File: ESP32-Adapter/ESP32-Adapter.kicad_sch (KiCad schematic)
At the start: 17 parts, among them J10 Barrel_Jack, J12 Conn_01x05, J13 Conn_01x05, J2 Conn_01x03, J3 Conn_01x03, J5 Conn_01x03, U1 ESP32-C5-DevKitC-1, U2 LM317DCYR, U3 Adafruit CANPAL, U4 ADAFRUIT INA219 BREAKOUT

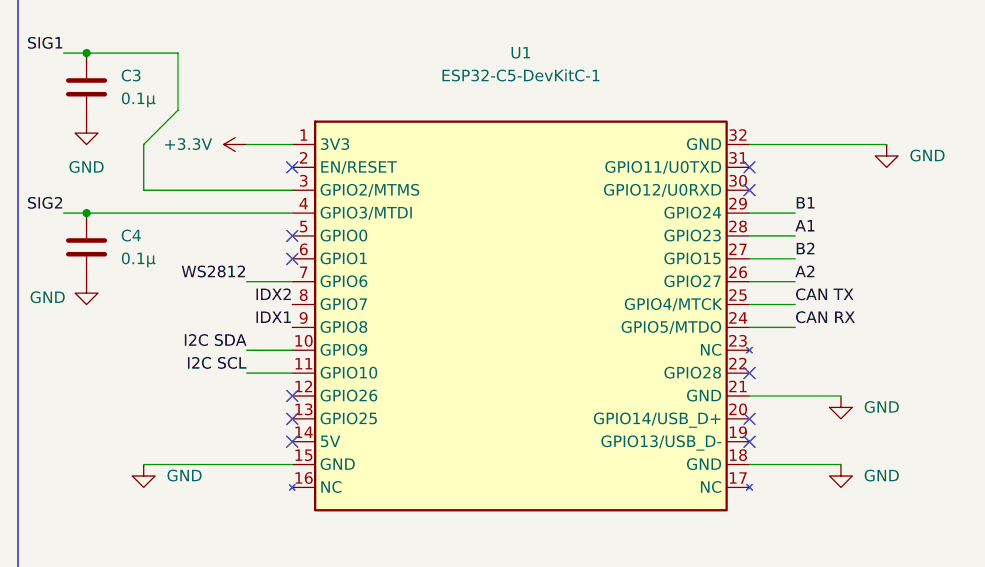
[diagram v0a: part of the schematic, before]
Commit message: fix schematic, symbols, footprints
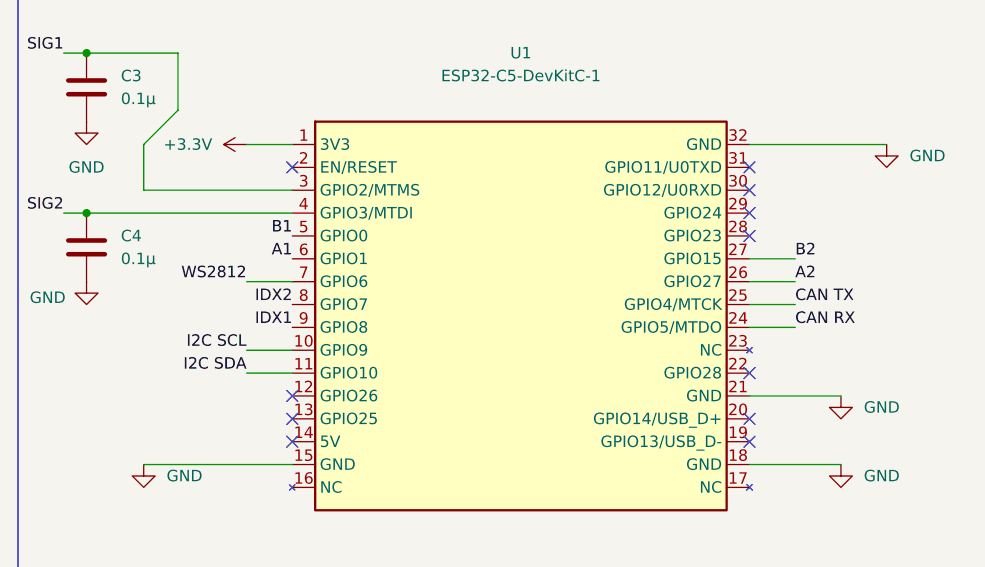
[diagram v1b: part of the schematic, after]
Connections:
- net A1: now also U1.6 (GPIO1); no longer U1.28 (GPIO23)
- net B1: now also U1.5 (GPIO0); no longer U1.29 (GPIO24)
- net I2C SCL: now also U1.10 (GPIO9); no longer U1.11 (GPIO10)
- net I2C SDA: now also U1.11 (GPIO10); no longer U1.10 (GPIO9)
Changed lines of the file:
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@@
+	)
+	(no_connect
+		(at 215.9 148.59)
 	)
 	(no_connect
@@
 	)
 	(no_connect
+		(at 215.9 146.05)
+	)
+	(no_connect
 		(at 165.1 171.45)
 	)
@@
 	)
 	(no_connect
-		(at 165.1 148.59)
-	)
-	(no_connect
 		(at 165.1 168.91)
 	)
@@
 	)
 	(no_connect
-		(at 165.1 151.13)
-	)
-	(no_connect
 		(at 110.49 179.07)
 	)
@@
 	(wire
 		(pts
-			(xy 215.9 146.05) (xy 220.98 146.05)
-		)
-		(stroke
-			(width 0)
-			(type default)
-		)
-	)
-	(wire
-		(pts
 			(xy 215.9 138.43) (xy 231.14 138.43)
 		)
@@
 		(pts
 			(xy 160.02 153.67) (xy 165.1 153.67)
-		)
-		(stroke
-			(width 0)
-			(type default)
-		)
-	)
-	(wire
-		(pts
-			(xy 215.9 148.59) (xy 220.98 148.59)
 		)
 		(stroke
@@
 		)
 	)
-	(label "I2C SCL"
-		(at 160.02 163.83 180)
-		(effects
-			(font
-				(size 1.27 1.27)
-			)
-			(justify right bottom)
-		)
-	)
-	(label "B1"
-		(at 220.98 146.05 0)
-		(effects
-			(font
-				(size 1.27 1.27)
-			)
-			(justify left bottom)
-		)
-	)
 	(label "B2"
 		(at 111.76 158.75 0)
@@
 	)
 	(label "B1"
+		(at 165.1 148.59 180)
+		(effects
+			(font
+				(size 1.27 1.27)
+			)
+			(justify right bottom)
+		)
+	)
+	(label "B1"
 		(at 111.76 143.51 0)
 		(effects
@@
 		)
 	)
+	(label "I2C SDA"
+		(at 160.02 163.83 180)
+		(effects
+			(font
+				(size 1.27 1.27)
+			)
+			(justify right bottom)
+		)
+	)
 	(label "B2"
 		(at 220.98 151.13 0)
@@
 		)
 	)
-	(label "A1"
-		(at 220.98 148.59 0)
-		(effects
-			(font
-				(size 1.27 1.27)
-			)
-			(justify left bottom)
-		)
-	)
 	(label "CAN TX"
 		(at 220.98 156.21 0)
@@
 		)
 	)
+	(label "A1"
+		(at 165.1 151.13 180)
+		(effects
+			(font
+				(size 1.27 1.27)
+			)
+			(justify right bottom)
+		)
+	)
 	(label "I2C SCL"
 		(at 273.05 193.04 180)
@@
 		)
 	)
+	(label "I2C SCL"
+		(at 160.02 161.29 180)
+		(effects
+			(font
+				(size 1.27 1.27)
+			)
+			(justify right bottom)
+		)
+	)
 	(label "IDX1"
 		(at 111.76 138.43 0)
@@
 		)
 	)
-	(label "I2C SDA"
-		(at 160.02 161.29 180)
-		(effects
-			(font
-				(size 1.27 1.27)
-			)
-			(justify right bottom)
-		)
-	)

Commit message: updates updates
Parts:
- removed C3, C4: 0.1µ, Capacitor_SMD:C_0402_1005Metric, symbol Device:C
- removed J2, J3: Conn_01x03, Connector_JST:JST_XH_S3B-XH-A-1_1x03_P2.50mm_Horizontal, symbol Connector_Generic:Conn_01x03
- removed U1: ESP32-C5-DevKitC-1, PCM_Espressif:ESP32-C5-DevKitC-1, symbol PCM_Espressif:ESP32-C5-DevKitC-1
- added J1, J2, J3: last resort, symbol Connector:Conn_01x01_Socket
- added U1: ICM-42670-P_Click, symbol Sensor_Motion:ICM-42670-P_Click
- added U5: ESP32-S3-DevKitC, PCM_Espressif:ESP32-S3-DevKitC, symbol PCM_Espressif:ESP32-S3-DevKitC
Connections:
- net +3.3V: now also U5.1 (3V3), U5.2 (3V3)
- net A1: now also U5.18 (GPIO12/ADC2_CH1)
- net A2: now also J13.2 (Pin_2), U5.19 (GPIO13/ADC2_CH2); no longer J12.3 (Pin_3)
- net B1: now also J12.3 (Pin_3), U5.8 (GPIO15/ADC2_CH4/32K_P); no longer J13.2 (Pin_2)
- net B2: now also U5.9 (GPIO16/ADC2_CH5/32K_N)
- net CAN RX: now also U5.6 (GPIO6/ADC1_CH5)
- net CAN TX: now also U5.5 (GPIO5/ADC1_CH4)
- net GND: now also U1.16 (GND), U1.8 (GND), U5.22 (GND), U5.23 (GND), U5.24 (GND), U5.44 (GND)
- net I2C SCL: now also U5.15 (GPIO9/ADC1_CH8)
- net I2C SDA: now also U5.16 (GPIO10/ADC1_CH9)
- net WS2812: now also U5.10 (GPIO17/ADC2_CH6)
- net IDX1 renamed IDXA
- net IDXA: now also U5.17 (GPIO11/ADC2_CH0)
- net IDX2 renamed IDXB
- net IDXB: now also U5.7 (GPIO7/ADC1_CH6)
- new net: J1.1 (Pin_1), U5.32 (GPIO35)
- new net: J2.1 (Pin_1), U5.33 (GPIO36)
- new net: J3.1 (Pin_1), U5.34 (GPIO37)
- no-connect marks 16 -> 20
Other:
- note added: "ICM-42670 IMU"
- note removed: "Analog"
- note removed: "Analog 1"
- note removed: "Analog 2"
- note removed: "Vcc"
- moved on the sheet: C1, C2, D1, J10, J12, J13, J5, R1, R2, U2, U3, U4

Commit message: austne yun pins adjusted
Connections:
- net CAN RX: now also U5.41 (GPIO1/ADC1_CH0); no longer U5.6 (GPIO6/ADC1_CH5)
- net CAN TX: now also U5.40 (GPIO2/ADC1_CH1); no longer U5.5 (GPIO5/ADC1_CH4)
- net I2C SCL: no longer U5.15 (GPIO9/ADC1_CH8)
- net I2C SDA: no longer U5.16 (GPIO10/ADC1_CH9)
- net IMU SCL: now reaches U1.13 (SCL)
- net IMU SCL: now also U5.15 (GPIO9/ADC1_CH8)
- net IMU SDA: now reaches U1.14 (SDA)
- net IMU SDA: now also U5.16 (GPIO10/ADC1_CH9)
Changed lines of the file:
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@@
+		)
+	)
+	(label "IMU SCL"
+		(at 115.57 213.36 0)
+		(effects
+			(font
+				(size 1.27 1.27)
+			)
+			(justify left bottom)
 		)
 	)
 	(label "A2"
 		(at 111.76 125.73 0)
+		(effects
+			(font
+				(size 1.27 1.27)
+			)
+			(justify left bottom)
+		)
+	)
+	(label "IMU SDA"
+		(at 115.57 215.9 0)
+		(effects
+			(font
+				(size 1.27 1.27)
+			)
+			(justify left bottom)
+		)
+	)
+	(label "IMU SCL"
+		(at 212.09 175.26 0)
+		(effects
+			(font
+				(size 1.27 1.27)
+			)
+			(justify left bottom)
+		)
+	)
+	(label "CAN RX"
+		(at 212.09 154.94 0)
+		(effects
+			(font
+				(size 1.27 1.27)
+			)
+			(justify left bottom)
+		)
+	)
+	(label "IMU SDA"
+		(at 212.09 177.8 0)
 		(effects
 			(font
@@
 			)
 			(justify right bottom)
-		)
-	)
-	(label "I2C SCL"
-		(at 212.09 175.26 0)
-		(effects
-			(font
-				(size 1.27 1.27)
-			)
-			(justify left bottom)
 		)
 	)
@@
 		)
 	)
-	(label "CAN TX"
-		(at 212.09 165.1 0)
-		(effects
-			(font
-				(size 1.27 1.27)
-			)
-			(justify left bottom)
-		)
-	)
 	(label "B2"
 		(at 161.29 144.78 180)
@@
 			)
 			(justify right bottom)
+		)
+	)
+	(label "I2C SDA"
+		(at 222.25 217.17 0)
+		(effects
+			(font
+				(size 1.27 1.27)
+			)
+			(justify left bottom)
 		)
 	)
@@
 		)
 	)
-	(label "CAN RX"
-		(at 212.09 167.64 0)
+	(label "I2C SCL"
+		(at 222.25 214.63 0)
 		(effects
 			(font
@@
 		)
 	)
-	(label "I2C SDA"
-		(at 212.09 177.8 0)
+	(label "CAN TX"
+		(at 110.49 168.91 0)
 		(effects
 			(font
@@
 	)
 	(label "CAN TX"
-		(at 110.49 168.91 0)
+		(at 212.09 157.48 0)
 		(effects
 			(font

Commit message: connect v sensor pins:
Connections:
- net IMU SCL is gone; now on net I2C SCL: U1.13 (SCL), U5.15 (GPIO9/ADC1_CH8)
- net IMU SDA is gone; now on net I2C SDA: U1.14 (SDA), U5.16 (GPIO10/ADC1_CH9)
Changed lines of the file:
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@@
+	)
+	(junction
+		(at 218.44 177.8)
+		(diameter 0)
+		(color 0 0 0 0)
 	)
 	(junction
@@
 	)
 	(junction
+		(at 218.44 175.26)
+		(diameter 0)
+		(color 0 0 0 0)
+	)
+	(junction
 		(at 275.59 142.24)
 		(diameter 0)
@@
 	(wire
 		(pts
+			(xy 218.44 172.72) (xy 218.44 175.26)
+		)
+		(stroke
+			(width 0)
+			(type default)
+		)
+	)
+	(wire
+		(pts
 			(xy 290.83 128.27) (xy 290.83 129.54)
 		)
@@
 	(wire
 		(pts
+			(xy 226.06 175.26) (xy 218.44 175.26)
+		)
+		(stroke
+			(width 0)
+			(type default)
+		)
+	)
+	(wire
+		(pts
 			(xy 111.76 143.51) (xy 116.84 143.51)
 		)
@@
 	(wire
 		(pts
+			(xy 218.44 180.34) (xy 226.06 180.34)
+		)
+		(stroke
+			(width 0)
+			(type default)
+		)
+	)
+	(wire
+		(pts
 			(xy 257.81 214.63) (xy 273.05 214.63)
 		)
@@
 	(wire
 		(pts
+			(xy 218.44 177.8) (xy 212.09 177.8)
+		)
+		(stroke
+			(width 0)
+			(type default)
+		)
+	)
+	(wire
+		(pts
 			(xy 304.8 142.24) (xy 313.69 142.24)
 		)
@@
 	(wire
 		(pts
+			(xy 226.06 177.8) (xy 218.44 177.8)
+		)
+		(stroke
+			(width 0)
+			(type default)
+		)
+	)
+	(wire
+		(pts
 			(xy 262.89 142.24) (xy 264.16 142.24)
 		)
@@
 	(wire
 		(pts
+			(xy 218.44 177.8) (xy 218.44 180.34)
+		)
+		(stroke
+			(width 0)
+			(type default)
+		)
+	)
+	(wire
+		(pts
 			(xy 111.76 128.27) (xy 116.84 128.27)
 		)
@@
 		(pts
 			(xy 275.59 118.11) (xy 290.83 118.11)
+		)
+		(stroke
+			(width 0)
+			(type default)
+		)
+	)
+	(wire
+		(pts
+			(xy 218.44 175.26) (xy 212.09 175.26)
+		)
+		(stroke
+			(width 0)
+			(type default)
+		)
+	)
+	(wire
+		(pts
+			(xy 226.06 172.72) (xy 218.44 172.72)
 		)
 		(stroke
@@
 	)
 	(label "IMU SCL"
-		(at 212.09 175.26 0)
+		(at 226.06 172.72 0)
 		(effects
 			(font
@@
 	)
 	(label "IMU SDA"
-		(at 212.09 177.8 0)
+		(at 226.06 177.8 0)
 		(effects
 			(font
@@
 	)
 	(label "I2C SDA"
-		(at 222.25 217.17 0)
+		(at 226.06 180.34 0)
 		(effects
 			(font
@@
 	)
 	(label "I2C SCL"
-		(at 222.25 214.63 0)
-		(effects
-			(font
+		(at 226.06 175.26 0)
+		(effects
+			(font

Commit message: esp32s3 pcb finish prelim
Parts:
- removed J1, J2, J3: last resort, symbol Connector:Conn_01x01_Socket
- U1: footprint (none) -> Connector_PinHeader_2.54mm:ICM-42670
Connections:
- net +3.3V: now also U1.7 (3V3)
- net A2: now also U5.17 (GPIO11/ADC2_CH0); no longer U5.19 (GPIO13/ADC2_CH2)
- net B2: now also U5.7 (GPIO7/ADC1_CH6); no longer U5.9 (GPIO16/ADC2_CH5/32K_N)
- net CAN RX: now also U5.40 (GPIO2/ADC1_CH1); no longer U5.41 (GPIO1/ADC1_CH0)
- net CAN TX: now also U5.41 (GPIO1/ADC1_CH0); no longer U5.40 (GPIO2/ADC1_CH1)
- net IDXA: now also U5.19 (GPIO13/ADC2_CH2); no longer U5.17 (GPIO11/ADC2_CH0)
- net IDXB: now also U5.9 (GPIO16/ADC2_CH5/32K_N); no longer U5.7 (GPIO7/ADC1_CH6)
- no-connect marks 20 -> 28
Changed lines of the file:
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@@
+	)
+	(no_connect
+		(at 95.25 205.74)
+	)
+	(no_connect
+		(at 95.25 208.28)
 	)
 	(no_connect
@@
 	)
 	(no_connect
+		(at 95.25 215.9)
+	)
+	(no_connect
 		(at 212.09 208.28)
 	)
@@
 	)
 	(no_connect
+		(at 95.25 213.36)
+	)
+	(no_connect
 		(at 161.29 157.48)
 	)
@@
 	)
 	(no_connect
+		(at 115.57 205.74)
+	)
+	(no_connect
 		(at 212.09 142.24)
 	)
@@
 	(no_connect
 		(at 212.09 144.78)
+	)
+	(no_connect
+		(at 115.57 203.2)
+	)
+	(no_connect
+		(at 95.25 210.82)
+	)
+	(no_connect
+		(at 95.25 203.2)
 	)
 	(no_connect
@@
 		)
 	)
+	(label "CAN RX"
+		(at 212.09 157.48 0)
+		(effects
+			(font
+				(size 1.27 1.27)
+			)
+			(justify left bottom)
+		)
+	)
 	(label "B2"
 		(at 111.76 140.97 0)
@@
 		)
 	)
-	(label "CAN RX"
-		(at 212.09 154.94 0)
+	(label "IDXA"
+		(at 212.09 185.42 0)
+		(effects
+			(font
+				(size 1.27 1.27)
+			)
+			(justify left bottom)
+		)
+	)
+	(label "A2"
+		(at 212.09 180.34 0)
 		(effects
 			(font
@@
 		)
 	)
+	(label "B2"
+		(at 212.09 170.18 0)
+		(effects
+			(font
+				(size 1.27 1.27)
+			)
+			(justify left bottom)
+		)
+	)
 	(label "B1"
 		(at 161.29 142.24 180)
@@
 		)
 	)
-	(label "B2"
+	(label "IDXB"
 		(at 161.29 144.78 180)
 		(effects
@@
 		)
 	)
-	(label "A2"
-		(at 212.09 185.42 0)
-		(effects
-			(font
-				(size 1.27 1.27)
-			)
-			(justify left bottom)
-		)
-	)
 	(label "I2C SCL"
 		(at 226.06 175.26 0)
@@
 		)
 	)
+	(label "CAN TX"
+		(at 212.09 154.94 0)
+		(effects
+			(font
+				(size 1.27 1.27)
+			)
+			(justify left bottom)
+		)
+	)
 	(label "WS2812"
 		(at 269.24 182.88 180)
@@
 		)
 	)
-	(label "CAN TX"
-		(at 212.09 157.48 0)
-		(effects
-			(font
-				(size 1.27 1.27)
-			)
-			(justify left bottom)
-		)
-	)
 	(label "IDXA"
 		(at 111.76 120.65 0)
@@
 		)
 	)
-	(label "IDXB"
-		(at 212.09 170.18 0)
-		(effects
-			(font
-				(size 1.27 1.27)
-			)
-			(justify left bottom)
-		)
-	)
-	(label "IDXA"
-		(at 212.09 180.34 0)
-		(effects
-			(font
-				(size 1.27 1.27)
-			)
-			(justify left bottom)
-		)
-	)
 	(label "B1"
 		(at 111.76 138.43 0)
@@
 	)
 	(symbol
-		(lib_id "Connector:Conn_01x01_Socket")
-		(at 217.17 198.12 0)
-		(unit 1)
-		(exclude_from_sim no)
-		(in_bom yes)
-		(on_board yes)
-		(dnp no)
-		(property "Reference" "J1"
-			(at 218.44 196.8499 0)
-			(effects
-				(font
-					(size 1.27 1.27)
-				)
-				(justify left)
-				(hide yes)
-			)
-		)
-		(property "Value" "last resort"
-			(at 218.44 198.12 0)
-			(effects
-				(font
-					(size 1.27 1.27)
-				)
-				(justify left)
-			)
-		)
-		(property "Footprint" ""
-			(at 217.17 198.12 0)
-			(effects
-				(font
-					(size 1.27 1.27)
-				)
-				(hide yes)
-			)
-		)
-		(property "Datasheet" "~"
-			(at 217.17 198.12 0)
-			(effects
-				(font
-					(size 1.27 1.27)
-				)
-				(hide yes)
-			)
-		)
-		(property "Description" "Generic connector, single row, 01x01, script generated"
-			(at 217.17 198.12 0)
-			(effects
-				(font
-					(size 1.27 1.27)
-				)
-				(hide yes)
-			)
-		)
-		(pin "1"
-		)
-		(instances
-			(project ""
-				(path "/69a61e70-b602-4412-b60e-1eedbaac8100"
-					(reference "J1")
-					(unit 1)
-				)
-			)
-		)
-	)
-	(symbol
 		(lib_id "Device:R")
 		(at 281.94 133.35 0)
@@
 	)
 	(symbol
+		(lib_id "power:+3.3V")
+		(at 95.25 218.44 90)
+		(unit 1)
+		(exclude_from_sim no)
+		(in_bom yes)
+		(on_board yes)
+		(dnp no)
+		(fields_autoplaced yes)
+		(property "Reference" "#PWR017"
+			(at 99.06 218.44 0)
+			(effects
+				(font
+					(size 1.27 1.27)
+				)
+				(hide yes)
+			)
+		)
+		(property "Value" "+3.3V"
+			(at 91.44 218.4399 90)
+			(effects
+				(font
+					(size 1.27 1.27)
+				)
+				(justify left)
+			)
+		)
+		(property "Footprint" ""
+			(at 95.25 218.44 0)
+			(effects
+				(font
+					(size 1.27 1.27)
+				)
+				(hide yes)
+			)
+		)
+		(property "Datasheet" ""
+			(at 95.25 218.44 0)
+			(effects
+				(font
+					(size 1.27 1.27)
+				)
+				(hide yes)
+			)
+		)
+		(property "Description" "Power symbol creates a global label with name \"+3.3V\""
+			(at 95.25 218.44 0)
+			(effects
+				(font
+					(size 1.27 1.27)
+				)
+				(hide yes)
+			)
+		)
+		(pin "1"
+		)
+		(instances
+			(project "ESP32-Adapter"
+				(path "/69a61e70-b602-4412-b60e-1eedbaac8100"
+					(reference "#PWR017")
+					(unit 1)
+				)
+			)
+		)
+	)
+	(symbol
 		(lib_id "power:GND")
 		(at 257.81 214.63 0)
@@
 			)
 		)
-		(property "Footprint" ""
+		(property "Footprint" "Connector_PinHeader_2.54mm:ICM-42670"
 			(at 105.41 199.39 0)
 			(effects
@@
 					(size 1.27 1.27)
 				)
-				(hide yes)
 			)
 		)
@@
 	)
 	(symbol
-		(lib_id "Connector:Conn_01x01_Socket")
-		(at 217.17 200.66 0)
-		(unit 1)
-		(exclude_from_sim no)
-		(in_bom yes)
-		(on_board yes)
-		(dnp no)
-		(property "Reference" "J2"
-			(at 218.44 199.3899 0)
-			(effects
-				(font
-					(size 1.27 1.27)
-				)
-				(justify left)
-				(hide yes)
-			)
-		)
-		(property "Value" "last resort"
-			(at 218.44 200.66 0)
-			(effects
-				(font
-					(size 1.27 1.27)
-				)
-				(justify left)
-			)
-		)
-		(property "Footprint" ""
-			(at 217.17 200.66 0)
-			(effects
-				(font
-					(size 1.27 1.27)
-				)
-				(hide yes)
-			)
-		)
-		(property "Datasheet" "~"
-			(at 217.17 200.66 0)
-			(effects
-				(font
-					(size 1.27 1.27)
-				)
-				(hide yes)
-			)
-		)
-		(property "Description" "Generic connector, single row, 01x01, script generated"
-			(at 217.17 200.66 0)
-			(effects
-				(font
-					(size 1.27 1.27)
-				)
-				(hide yes)
-			)
-		)
-		(pin "1"
-		)
-		(instances
-			(project "ESP32-Adapter"
-				(path "/69a61e70-b602-4412-b60e-1eedbaac8100"
-					(reference "J2")
-					(unit 1)
-				)
-			)
-		)
-	)
-	(symbol
 		(lib_id "Device:C")
 		(at 304.8 146.05 0)
@@
 					(unit 1)
 				)
-			)
-		)
-	)
-	(symbol
-		(lib_id "Connector:Conn_01x01_Socket")
-		(at 217.17 203.2 0)
-		(unit 1)
-		(exclude_from_sim no)
-		(in_bom yes)
-		(on_board yes)
-		(dnp no)
-		(property "Reference" "J3"
-			(at 218.44 201.9299 0)
-			(effects
-				(font
-					(size 1.27 1.27)
-				)
-				(justify left)
-				(hide yes)
-			)
-		)
-		(property "Value" "last resort"
-			(at 218.44 203.2 0)
-			(effects
-				(font
-					(size 1.27 1.27)
-				)
-				(justify left)
-			)
-		)
-		(property "Footprint" ""
-			(at 217.17 203.2 0)
-			(effects
-				(font
-					(size 1.27 1.27)
-				)
-				(hide yes)
-			)
-		)
-		(property "Datasheet" "~"
-			(at 217.17 203.2 0)
-			(effects
-				(font
-					(size 1.27 1.27)
-				)
-				(hide yes)
-			)
-		)
-		(property "Description" "Generic connector, single row, 01x01, script generated"
-			(at 217.17 203.2 0)
-			(effects
-				(font
-					(size 1.27 1.27)
-				)
-				(hide yes)
-			)
-		)
-		(pin "1"
-		)
-		(instances
-			(project "ESP32-Adapter"
-				(path "/69a61e70-b602-4412-b60e-1eedbaac8100"
-					(reference "J3")
-					(unit 1)
-				)
